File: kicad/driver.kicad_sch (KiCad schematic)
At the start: 72 parts, among them Q1 IRFZ44NPBF, Q2 IRFZ44NPBF, Q3 IRFZ44NPBF, Q4 IRFZ44NPBF, Q5 IRFZ44NPBF, Q6 IRFZ44NPBF, U1 ir2104, U2 ir2104, U3 ir2104, U4 INA180A2IDBVR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

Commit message: [kicad] Rechecked all footprints and components requirements | TODO: think about replacing the ESD package with something else [simulations] Checked simulations of buck converter with reality
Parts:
- C10, C11, C12, C13, C14, C15, C7, C8, C9: MFR.Part (none) -> CL05B103KB5NNNC
- C16, C17, C18: MFR.Part (none) -> ERS1HM471G20OT
- C19, C20, C21: footprint Resistor_SMD:R_0402_1005Metric -> Capacitor_SMD:C_0402_1005Metric; MFR.Part (none) -> CL05B104KB54PNC
- C4, C5, C6: MFR.Part (none) -> CL10A475KO8NNNC
- R13: MFR.Part (none) -> 0603WAF100KT5E; jlcpcb (none) -> C22936
- R14, R15, R16, R17, R18, R19, R20, R21: MFR.Part (none) -> 0603WAF100KT5E
- R22, R23, R24, R25, R26, R27, R28, R29, R30, R31, R32, R33: MFR.Part (none) -> 0603WAF3302T5E
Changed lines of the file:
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@@
+      (effects (font (size 1.27 1.27)) hide)
+    )
+    (property "MFR.Part" "0603WAF3302T5E" (at 181.61 30.48 0)
       (effects (font (size 1.27 1.27)) hide)
     )
@@
       (effects (font (size 1.27 1.27)) hide)
     )
+    (property "MFR.Part" "0603WAF3302T5E" (at 161.925 50.8 0)
+      (effects (font (size 1.27 1.27)) hide)
+    )
     (pin "2")
     (pin "1")
@@
     )
     (property "jlcpcb" "C4216" (at 171.45 50.8 0)
+      (effects (font (size 1.27 1.27)) hide)
+    )
+    (property "MFR.Part" "0603WAF3302T5E" (at 171.45 50.8 0)
       (effects (font (size 1.27 1.27)) hide)
     )
@@
       (effects (font (size 1.27 1.27)) hide)
     )
+    (property "MFR.Part" "0603WAF100KT5E" (at 99.695 123.825 0)
+      (effects (font (size 1.27 1.27)) hide)
+    )
     (pin "1")
     (pin "2")
@@
       (effects (font (size 1.27 1.27)) hide)
     )
+    (property "MFR.Part" "0603WAF100KT5E" (at 116.84 163.83 0)
+      (effects (font (size 1.27 1.27)) hide)
+    )
     (pin "1")
     (pin "2")
@@
     )
     (property "jlcpcb" "C15195" (at 115.57 59.69 0)
+      (effects (font (size 1.27 1.27)) hide)
+    )
+    (property "MFR.Part" "CL05B103KB5NNNC" (at 115.57 59.69 0)
       (effects (font (size 1.27 1.27)) hide)
     )
@@
       (effects (font (size 1.27 1.27)) hide)
     )
+    (property "MFR.Part" "0603WAF3302T5E" (at 161.925 40.64 0)
+      (effects (font (size 1.27 1.27)) hide)
+    )
     (pin "2")
     (pin "1")
@@
       (effects (font (size 1.27 1.27)) hide)
     )
+    (property "MFR.Part" "CL10A475KO8NNNC" (at 64.77 105.41 0)
+      (effects (font (size 1.27 1.27)) hide)
+    )
     (pin "1")
     (pin "2")
@@
       (effects (font (size 1.27 1.27)) hide)
     )
+    (property "MFR.Part" "CL05B103KB5NNNC" (at 116.84 168.91 0)
+      (effects (font (size 1.27 1.27)) hide)
+    )
     (pin "2")
     (pin "1")
@@
       (effects (font (size 1.27 1.27)) hide)
     )
+    (property "MFR.Part" "0603WAF100KT5E" (at 107.315 58.42 0)
+      (effects (font (size 1.27 1.27)) hide)
+    )
     (pin "1")
     (pin "2")
@@
       (effects (font (size 1.27 1.27)) (justify left))
     )
-    (property "Footprint" "Resistor_SMD:R_0402_1005Metric" (at 260.985 87.63 0)
+    (property "Footprint" "Capacitor_SMD:C_0402_1005Metric" (at 260.985 87.63 0)
       (effects (font (size 1.27 1.27)) hide)
     )
@@
       (effects (font (size 1.27 1.27)) hide)
     )
+    (property "MFR.Part" "CL05B104KB54PNC" (at 260.985 87.63 0)
+      (effects (font (size 1.27 1.27)) hide)
+    )
     (pin "1")
     (pin "2")
@@
     )
     (property "jlcpcb" "C22936" (at 107.315 118.11 0)
+      (effects (font (size 1.27 1.27)) hide)
+    )
+    (property "MFR.Part" "0603WAF100KT5E" (at 107.315 118.11 0)
       (effects (font (size 1.27 1.27)) hide)
     )
@@
       (effects (font (size 1.27 1.27)) hide)
     )
+    (property "MFR.Part" "CL10A475KO8NNNC" (at 63.5 49.53 0)
+      (effects (font (size 1.27 1.27)) hide)
+    )
     (pin "1")
     (pin "2")
@@
     )
     (property "jlcpcb" "C4216" (at 204.47 48.26 90)
+      (effects (font (size 1.27 1.27)) hide)
+    )
+    (property "MFR.Part" "0603WAF3302T5E" (at 204.47 48.26 0)
       (effects (font (size 1.27 1.27)) hide)
     )
@@
       (effects (font (size 1.27 1.27)) hide)
     )
+    (property "MFR.Part" "0603WAF100KT5E" (at 108.585 168.91 0)
+      (effects (font (size 1.27 1.27)) hide)
+    )
     (pin "1")
     (pin "2")
@@
       (effects (font (size 1.27 1.27)) hide)
     )
+    (property "MFR.Part" "0603WAF3302T5E" (at 171.45 38.1 0)
+      (effects (font (size 1.27 1.27)) hide)
+    )
     (pin "2")
     (pin "1")
@@
       (effects (font (size 1.27 1.27)) hide)
     )
+    (property "MFR.Part" "0603WAF3302T5E" (at 161.925 31.75 0)
+      (effects (font (size 1.27 1.27)) hide)
+    )
     (pin "2")
     (pin "1")
@@
     )
     (property "jlcpcb" "C106666" (at 124.46 54.61 0)
+      (effects (font (size 1.27 1.27)) hide)
+    )
+    (property "MFR.Part" "ERS1HM471G20OT" (at 124.46 54.61 0)
       (effects (font (size 1.27 1.27)) hide)
     )
@@
       (effects (font (size 1.27 1.27)) hide)
     )
+    (property "MFR.Part" "0603WAF3302T5E" (at 181.61 50.8 0)
+      (effects (font (size 1.27 1.27)) hide)
+    )
     (pin "2")
     (pin "1")
@@
       (effects (font (size 1.27 1.27)) hide)
     )
+    (property "MFR.Part" "CL10A475KO8NNNC" (at 64.77 157.48 0)
+      (effects (font (size 1.27 1.27)) hide)
+    )
     (pin "1")
     (pin "2")
@@
       (effects (font (size 1.27 1.27)) hide)
     )
+    (property "MFR.Part" "CL05B103KB5NNNC" (at 107.315 123.19 0)
+      (effects (font (size 1.27 1.27)) hide)
+    )
     (pin "2")
     (pin "1")
@@
     )
     (property "jlcpcb" "C15195" (at 100.965 184.785 0)
+      (effects (font (size 1.27 1.27)) hide)
+    )
+    (property "MFR.Part" "CL05B103KB5NNNC" (at 100.965 184.785 0)
       (effects (font (size 1.27 1.27)) hide)
     )
@@
       (effects (font (size 1.27 1.27)) hide)
     )
+    (property "MFR.Part" "0603WAF100KT5E" (at 99.695 64.77 0)
+      (effects (font (size 1.27 1.27)) hide)
+    )
+    (property "jlcpcb" "C22936" (at 99.695 64.77 0)
+      (effects (font (size 1.27 1.27)) hide)
+    )
     (pin "1")
     (pin "2")
@@
       (effects (font (size 1.27 1.27)) hide)
     )
+    (property "MFR.Part" "0603WAF3302T5E" (at 204.47 43.18 0)
+      (effects (font (size 1.27 1.27)) hide)
+    )
     (pin "2")
     (pin "1")
@@
       (effects (font (size 1.27 1.27)) hide)
     )
+    (property "MFR.Part" "CL05B103KB5NNNC" (at 99.695 69.85 0)
+      (effects (font (size 1.27 1.27)) hide)
+    )
     (pin "2")
     (pin "1")
@@
     )
     (property "jlcpcb" "C15195" (at 108.585 173.99 0)
+      (effects (font (size 1.27 1.27)) hide)
+    )
+    (property "MFR.Part" "CL05B103KB5NNNC" (at 108.585 173.99 0)
       (effects (font (size 1.27 1.27)) hide)
     )
@@
       (effects (font (size 1.27 1.27)) hide)
     )
+    (property "MFR.Part" "0603WAF100KT5E" (at 115.57 50.8 0)
+      (effects (font (size 1.27 1.27)) hide)
+    )
     (pin "1")
     (pin "2")
@@
       (effects (font (size 1.27 1.27)) hide)
     )
+    (property "MFR.Part" "0603WAF3302T5E" (at 171.45 31.75 0)
+      (effects (font (size 1.27 1.27)) hide)
+    )
     (pin "2")
     (pin "1")
@@
       (effects (font (size 1.27 1.27)) hide)
     )
+    (property "MFR.Part" "0603WAF100KT5E" (at 115.57 113.03 0)
+      (effects (font (size 1.27 1.27)) hide)
+    )
     (pin "1")
     (pin "2")
@@
       (effects (font (size 1.27 1.27)) hide)
     )
+    (property "MFR.Part" "CL05B103KB5NNNC" (at 115.57 118.11 0)
+      (effects (font (size 1.27 1.27)) hide)
+    )
     (pin "2")
     (pin "1")
@@
       (effects (font (size 1.27 1.27)) (justify left))
     )
-    (property "Footprint" "Resistor_SMD:R_0402_1005Metric" (at 169.545 83.82 0)
+    (property "Footprint" "Capacitor_SMD:C_0402_1005Metric" (at 169.545 83.82 0)
       (effects (font (size 1.27 1.27)) hide)
     )
@@
       (effects (font (size 1.27 1.27)) hide)
     )
+    (property "MFR.Part" "CL05B104KB54PNC" (at 169.545 83.82 0)
+      (effects (font (size 1.27 1.27)) hide)
+    )
     (pin "1")
     (pin "2")
@@
     )
     (property "jlcpcb" "C106666" (at 125.73 168.91 0)
+      (effects (font (size 1.27 1.27)) hide)
+    )
+    (property "MFR.Part" "ERS1HM471G20OT" (at 125.73 168.91 0)
       (effects (font (size 1.27 1.27)) hide)
     )
@@
       (effects (font (size 1.27 1.27)) hide)
     )
+    (property "MFR.Part" "0603WAF3302T5E" (at 181.61 35.56 0)
+      (effects (font (size 1.27 1.27)) hide)
+    )
     (pin "2")
     (pin "1")
@@
     )
     (property "jlcpcb" "C4216" (at 204.47 38.1 90)
+      (effects (font (size 1.27 1.27)) hide)
+    )
+    (property "MFR.Part" "0603WAF3302T5E" (at 204.47 38.1 0)
       (effects (font (size 1.27 1.27)) hide)
     )
@@
       (effects (font (size 1.27 1.27)) hide)
     )
+    (property "MFR.Part" "CL05B103KB5NNNC" (at 107.315 63.5 0)
+      (effects (font (size 1.27 1.27)) hide)
+    )
     (pin "2")
     (pin "1")
@@
       (effects (font (size 1.27 1.27)) hide)
     )
+    (property "MFR.Part" "0603WAF100KT5E" (at 100.965 179.705 0)
+      (effects (font (size 1.27 1.27)) hide)
+    )
     (pin "1")
     (pin "2")
@@
       (effects (font (size 1.27 1.27)) (justify left))
     )
-    (property "Footprint" "Resistor_SMD:R_0402_1005Metric" (at 217.17 84.455 0)
+    (property "Footprint" "Capacitor_SMD:C_0402_1005Metric" (at 217.17 84.455 0)
       (effects (font (size 1.27 1.27)) hide)
     )
@@
     )
     (property "jlcpcb" "C307331" (at 217.17 84.455 0)
+      (effects (font (size 1.27 1.27)) hide)
+    )
+    (property "MFR.Part" "CL05B104KB54PNC" (at 217.17 84.455 0)
       (effects (font (size 1.27 1.27)) hide)
     )
@@
       (effects (font (size 1.27 1.27)) hide)
     )
+    (property "MFR.Part" "ERS1HM471G20OT" (at 124.46 111.76 0)
+      (effects (font (size 1.27 1.27)) hide)
+    )
     (pin "1")
     (pin "2")
@@
       (effects (font (size 1.27 1.27)) hide)
     )
+    (property "MFR.Part" "CL05B103KB5NNNC" (at 99.695 128.905 0)
+      (effects (font (size 1.27 1.27)) hide)
+    )

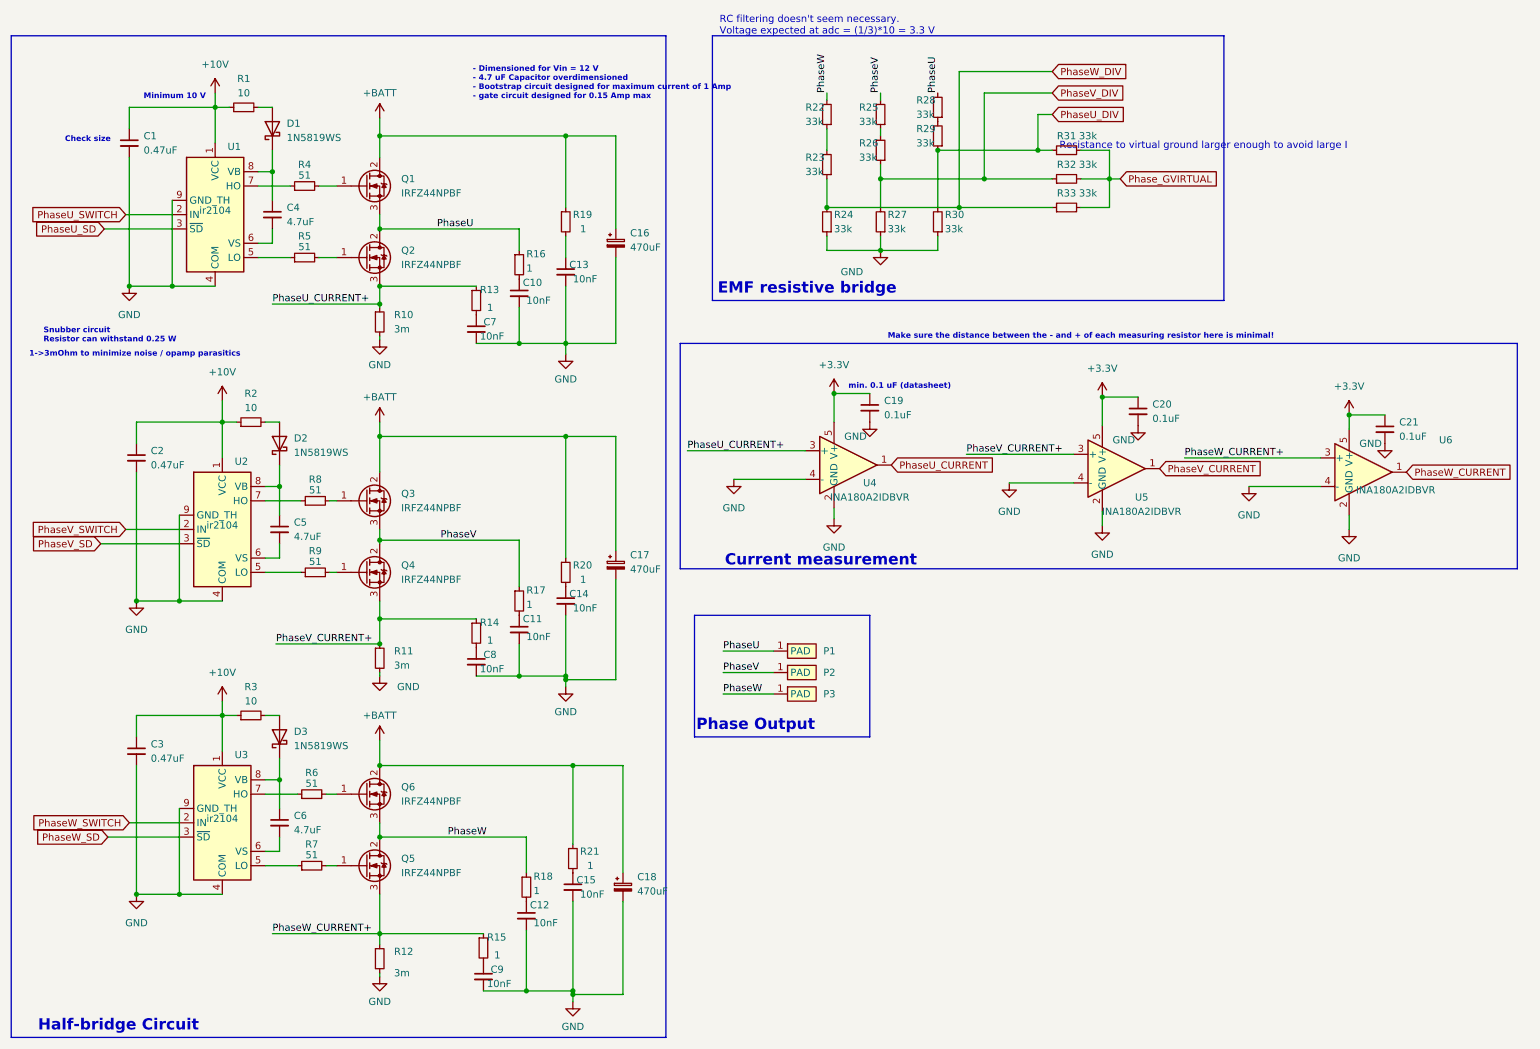
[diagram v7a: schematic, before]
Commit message: [kicad] Added different ESD protection device, silkscreen indication on the back, [review] Added pdf file and images of the front and back as well as 3d images
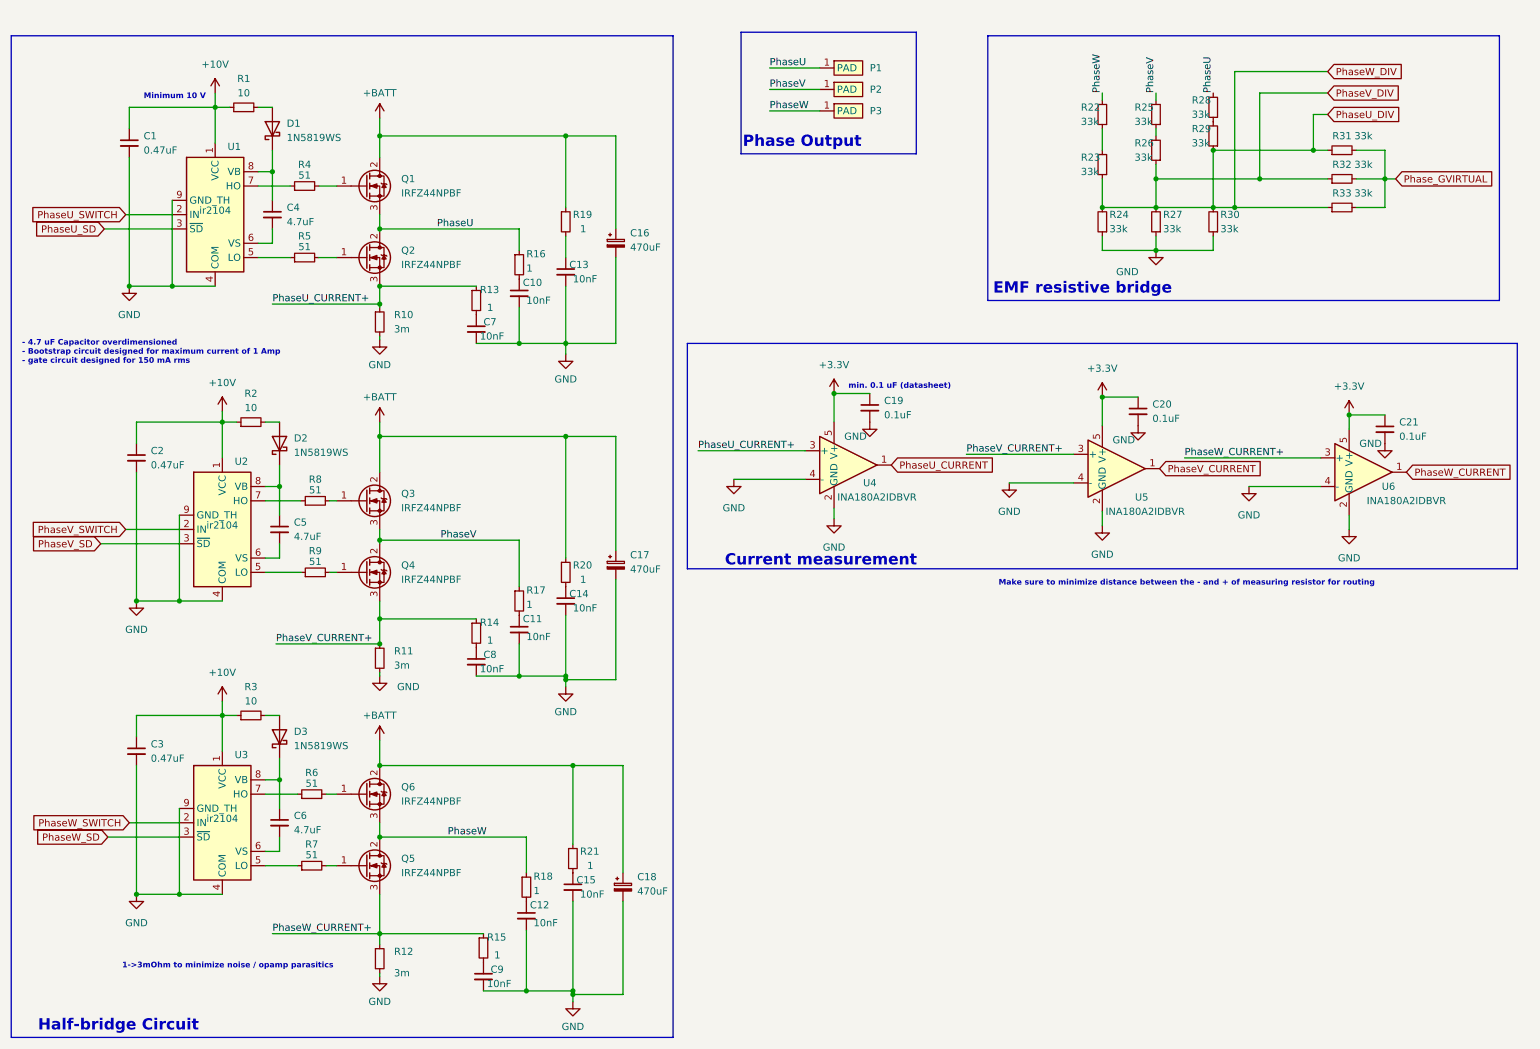
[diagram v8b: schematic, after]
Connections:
- net PhaseV_DIV is gone; now on net PhaseU_DIV: R26.1, R27.2, R32.1
- net PhaseW_DIV is gone; now on net PhaseU_DIV: R23.1, R24.2, R33.1
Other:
- note added: "- 4.7 uF Capacitor overdimensioned - Bootstrap circuit designed for maximum current of 1 Amp - gate circuit designed for 150 mA rms"
- note added: "Make sure to minimize distance between the - and + of measuring resistor for routing"
- note removed: "- Dimensioned for Vin = 12 V - 4.7 uF Capacitor overdimensioned - Bootstrap circuit designed for maximum current of 1 Amp - gate circuit designed for 0.15 Amp max"
- note removed: "Check size"
- note removed: "Make sure the distance between the - and + of each measuring resistor here is minimal!"
- note removed: "RC filtering doesn't seem necessary. Voltage expected at adc = (1/3)*10 = 3.3 V"
- note removed: "Resistance to virtual ground larger enough to avoid large I"
- note removed: "Snubber circuit Resistor can withstand 0.25 W"
- company: Igor Wolfs -> IW
- moved on the sheet: P1, P2, P3, R22, R23, R24, R25, R26, R27, R28, R29, R30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
